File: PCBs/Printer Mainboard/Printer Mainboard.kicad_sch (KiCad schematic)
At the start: 4 parts

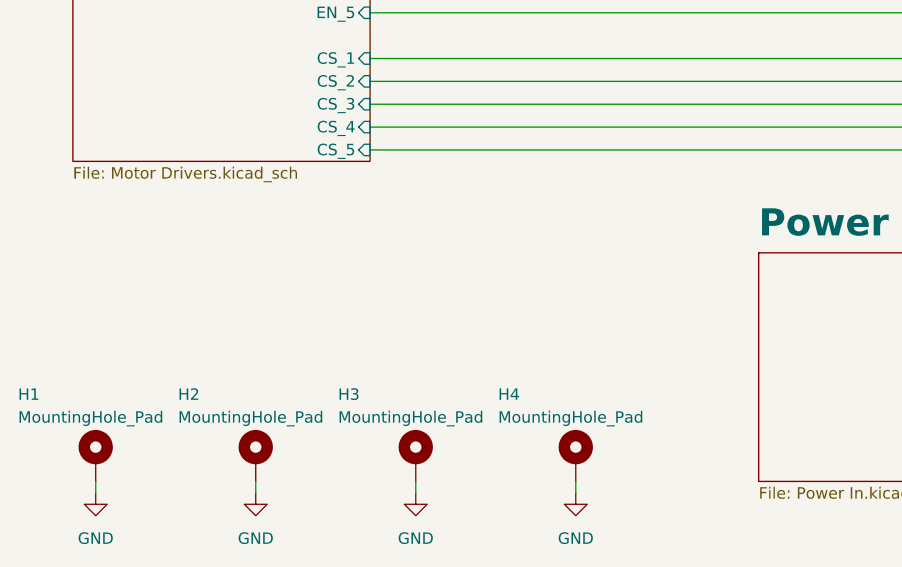
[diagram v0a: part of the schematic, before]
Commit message: Updated KiCad files and made 3D files for expansion board and thermister board
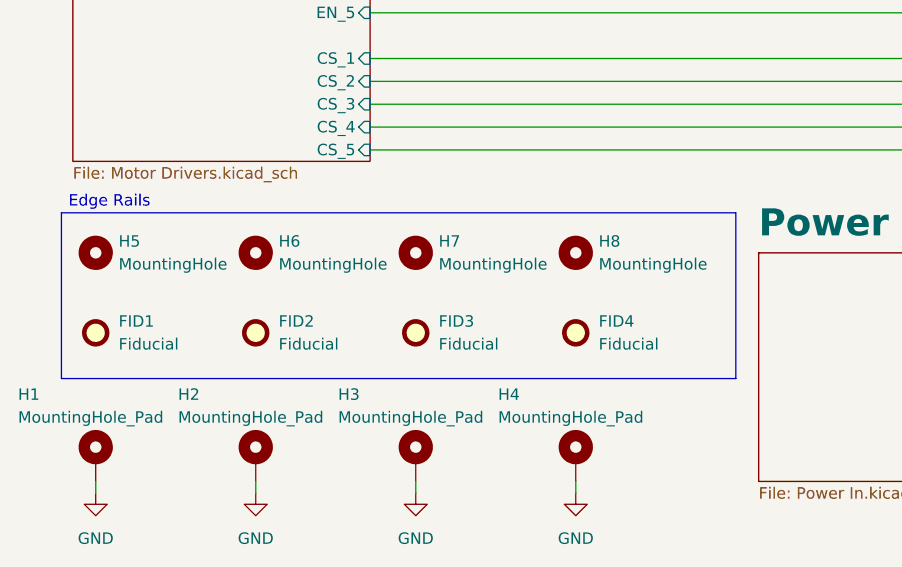
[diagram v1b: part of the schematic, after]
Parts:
- added FID1, FID2, FID3, FID4: Fiducial, Fiducial:Fiducial_0.5mm_Mask1.5mm, symbol Mechanical:Fiducial
- added H5, H6, H7, H8: MountingHole, MountingHole:MountingHole_2mm, symbol Mechanical:MountingHole
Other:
- note added: "Edge Rails"
